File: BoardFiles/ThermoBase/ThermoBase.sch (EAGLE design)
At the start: 31 parts, among them CON1 BARREL_JACK_3PIN, U1 MOSFET_N, U2 MOSFET_N, U3 MOSFET_N, U4 LM317

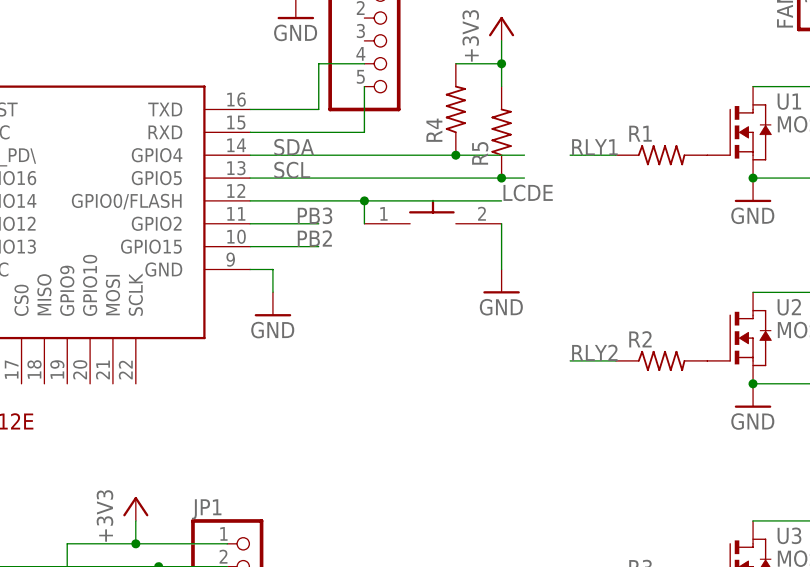
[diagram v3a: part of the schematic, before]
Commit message: Found some board errors and got an AC demo ready
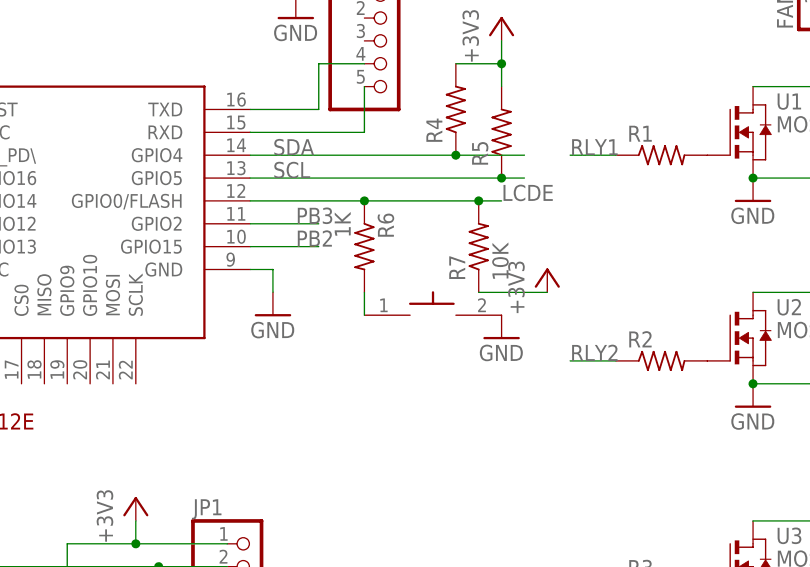
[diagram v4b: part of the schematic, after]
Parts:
- added R6: 1K, DR:R-US_R0805
- added R7: 10K, DR:R-US_R0805
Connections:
- new net N$16: BTN1.P$1, R6.2
- net +3V3: now also R7.1
- net LCDE: now also R6.1, R7.2; no longer BTN1.P$1
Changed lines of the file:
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@@
 <part name="+3V6" library="supply1" library_urn="urn:adsk.eagle:library:371" deviceset="+3V3" device=""/>
 <part name="GND12" library="supply1" library_urn="urn:adsk.eagle:library:371" deviceset="GND" device=""/>
+<part name="R6" library="DR" deviceset="R-US_" device="R0805" value="1K"/>
+<part name="R7" library="DR" deviceset="R-US_" device="R0805" value="10K"/>
+<part name="+3V7" library="supply1" library_urn="urn:adsk.eagle:library:371" deviceset="+3V3" device=""/>
 </parts>
 <sheets>
@@
 <attribute name="VALUE" x="91.44" y="60.96" size="1.778" layer="96"/>
 </instance>
-<instance part="BTN1" gate="G$1" x="109.22" y="40.64" smashed="yes"/>
-<instance part="GND2" gate="1" x="116.84" y="33.02" smashed="yes">
-<attribute name="VALUE" x="114.3" y="30.48" size="1.778" layer="96"/>
+<instance part="BTN1" gate="G$1" x="109.22" y="30.48" smashed="yes"/>
+<instance part="GND2" gate="1" x="116.84" y="27.94" smashed="yes">
+<attribute name="VALUE" x="114.3" y="25.4" size="1.778" layer="96"/>
 </instance>
 <instance part="+3V1" gate="G$1" x="45.72" y="58.42" smashed="yes">
@@
 <instance part="GND12" gate="1" x="60.96" y="0" smashed="yes">
 <attribute name="VALUE" x="58.42" y="-2.54" size="1.778" layer="96"/>
+</instance>
+<instance part="R6" gate="G$1" x="101.6" y="38.1" smashed="yes" rot="R270">
+<attribute name="NAME" x="103.0986" y="41.91" size="1.778" layer="95" rot="R270"/>
+<attribute name="VALUE" x="98.298" y="41.91" size="1.778" layer="96" rot="R270"/>
+</instance>
+<instance part="R7" gate="G$1" x="114.3" y="38.1" smashed="yes" rot="R90">
+<attribute name="NAME" x="112.8014" y="34.29" size="1.778" layer="95" rot="R90"/>
+<attribute name="VALUE" x="117.602" y="34.29" size="1.778" layer="96" rot="R90"/>
+</instance>
+<instance part="+3V7" gate="G$1" x="121.92" y="35.56" smashed="yes">
+<attribute name="VALUE" x="119.38" y="30.48" size="1.778" layer="96" rot="R90"/>
 </instance>
 </instances>
@@
 <pinref part="BTN1" gate="G$1" pin="P$2"/>
 <pinref part="GND2" gate="1" pin="GND"/>
-<wire x1="116.84" y1="35.56" x2="116.84" y2="40.64" width="0.1524" layer="91"/>
 </segment>
 <segment>
@@
 <wire x1="68.58" y1="-12.7" x2="86.36" y2="-12.7" width="0.1524" layer="91"/>
 </segment>
+<segment>
+<pinref part="+3V7" gate="G$1" pin="+3V3"/>
+<pinref part="R7" gate="G$1" pin="1"/>
+<wire x1="121.92" y1="33.02" x2="114.3" y2="33.02" width="0.1524" layer="91"/>
+</segment>
 </net>
 <net name="SDA" class="0">
@@
 </segment>
 <segment>
-<pinref part="BTN1" gate="G$1" pin="P$1"/>
 <pinref part="U$1" gate="G$1" pin="GPIO0/FLASH"/>
-<wire x1="101.6" y1="40.64" x2="101.6" y2="43.18" width="0.1524" layer="91"/>
-<wire x1="101.6" y1="43.18" x2="88.9" y2="43.18" width="0.1524" layer="91"/>
-<wire x1="101.6" y1="43.18" x2="116.84" y2="43.18" width="0.1524" layer="91"/>
+<wire x1="88.9" y1="43.18" x2="101.6" y2="43.18" width="0.1524" layer="91"/>
+<label x="116.84" y="43.18" size="1.778" layer="95"/>
+<pinref part="R6" gate="G$1" pin="1"/>
+<wire x1="101.6" y1="43.18" x2="114.3" y2="43.18" width="0.1524" layer="91"/>
 <junction x="101.6" y="43.18"/>
-<label x="116.84" y="43.18" size="1.778" layer="95"/>
+<pinref part="R7" gate="G$1" pin="2"/>
+<wire x1="114.3" y1="43.18" x2="116.84" y2="43.18" width="0.1524" layer="91"/>
+<junction x="114.3" y="43.18"/>
 </segment>
 </net>
@@
 </segment>
 </net>
+<net name="N$16" class="0">
+<segment>
+<pinref part="BTN1" gate="G$1" pin="P$1"/>
+<pinref part="R6" gate="G$1" pin="2"/>
+<wire x1="101.6" y1="30.48" x2="101.6" y2="33.02" width="0.1524" layer="91"/>
+</segment>
+</net>

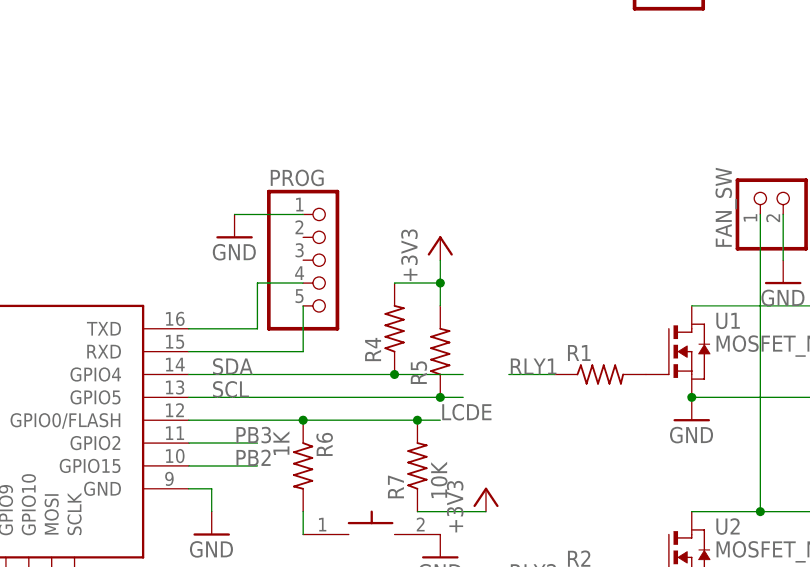
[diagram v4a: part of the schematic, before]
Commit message: Ordered boards V1.0
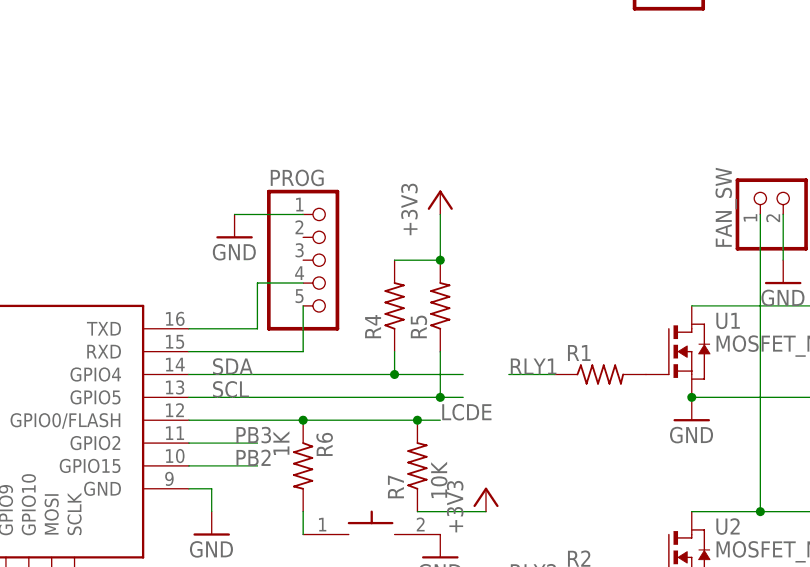
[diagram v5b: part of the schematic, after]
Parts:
- CON1: value BARREL_JACK_3PIN -> BARREL_JACK_3PINPJ-102A_2MM_HOLES; device DR:BARREL_JACK_3PIN -> DR:BARREL_JACK_3PINPJ-102A_2MM_HOLES
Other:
- moved on the sheet: R4, R5
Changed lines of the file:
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@@
 <layer number="56" name="wert" color="7" fill="1" visible="no" active="no"/>
 <layer number="57" name="tCAD" color="7" fill="1" visible="no" active="no"/>
+<layer number="88" name="SimResults" color="9" fill="1" visible="no" active="no"/>
+<layer number="89" name="SimProbes" color="9" fill="1" visible="no" active="no"/>
 <layer number="90" name="Modules" color="5" fill="1" visible="no" active="no"/>
 <layer number="91" name="Nets" color="2" fill="1" visible="yes" active="yes"/>
@@
 <part name="+3V3" library="supply1" library_urn="urn:adsk.eagle:library:371" deviceset="+3V3" device=""/>
 <part name="GND3" library="supply1" library_urn="urn:adsk.eagle:library:371" deviceset="GND" device=""/>
-<part name="CON1" library="DR" deviceset="BARREL_JACK_3PIN" device=""/>
+<part name="CON1" library="DR" deviceset="BARREL_JACK_3PIN" device="PJ-102A_2MM_HOLES" value="BARREL_JACK_3PINPJ-102A_2MM_HOLES"/>
 <part name="C1" library="DR" deviceset="C-US" device="C0805"/>
 <part name="C2" library="DR" deviceset="C-US" device="C0805"/>
@@
 <attribute name="VALUE" x="20.32" y="60.96" size="1.778" layer="96"/>
 </instance>
-<instance part="R4" gate="G$1" x="111.76" y="53.34" smashed="yes" rot="R90">
-<attribute name="NAME" x="110.2614" y="49.53" size="1.778" layer="95" rot="R90"/>
-<attribute name="VALUE" x="115.062" y="49.53" size="1.778" layer="96" rot="R90"/>
-</instance>
-<instance part="R5" gate="G$1" x="116.84" y="50.8" smashed="yes" rot="R90">
-<attribute name="NAME" x="115.3414" y="46.99" size="1.778" layer="95" rot="R90"/>
-<attribute name="VALUE" x="120.142" y="46.99" size="1.778" layer="96" rot="R90"/>
+<instance part="R4" gate="G$1" x="111.76" y="55.88" smashed="yes" rot="R90">
+<attribute name="NAME" x="110.2614" y="52.07" size="1.778" layer="95" rot="R90"/>
+<attribute name="VALUE" x="115.062" y="52.07" size="1.778" layer="96" rot="R90"/>
+</instance>
+<instance part="R5" gate="G$1" x="116.84" y="55.88" smashed="yes" rot="R90">
+<attribute name="NAME" x="115.3414" y="52.07" size="1.778" layer="95" rot="R90"/>
+<attribute name="VALUE" x="120.142" y="52.07" size="1.778" layer="96" rot="R90"/>
 </instance>
 <instance part="JP3" gate="A" x="20.32" y="10.16" smashed="yes">
@@
 <attribute name="VALUE" x="27.94" y="-5.08" size="1.778" layer="96"/>
 </instance>
-<instance part="+3V5" gate="G$1" x="116.84" y="63.5" smashed="yes">
-<attribute name="VALUE" x="114.3" y="58.42" size="1.778" layer="96" rot="R90"/>
+<instance part="+3V5" gate="G$1" x="116.84" y="68.58" smashed="yes">
+<attribute name="VALUE" x="114.3" y="63.5" size="1.778" layer="96" rot="R90"/>
 </instance>
 <instance part="RLY1" gate="G$1" x="190.5" y="58.42" smashed="yes">
@@
 <pinref part="R5" gate="G$1" pin="2"/>
 <pinref part="+3V5" gate="G$1" pin="+3V3"/>
-<wire x1="116.84" y1="55.88" x2="116.84" y2="58.42" width="0.1524" layer="91"/>
 <pinref part="R4" gate="G$1" pin="2"/>
-<wire x1="116.84" y1="58.42" x2="116.84" y2="60.96" width="0.1524" layer="91"/>
-<wire x1="116.84" y1="58.42" x2="111.76" y2="58.42" width="0.1524" layer="91"/>
-<junction x="116.84" y="58.42"/>
+<wire x1="116.84" y1="60.96" x2="116.84" y2="66.04" width="0.1524" layer="91"/>
+<wire x1="116.84" y1="60.96" x2="111.76" y2="60.96" width="0.1524" layer="91"/>
+<junction x="116.84" y="60.96"/>
 </segment>
 <segment>
@@
 <pinref part="R4" gate="G$1" pin="1"/>
 <wire x1="88.9" y1="48.26" x2="111.76" y2="48.26" width="0.1524" layer="91"/>
+<wire x1="111.76" y1="50.8" x2="111.76" y2="48.26" width="0.1524" layer="91"/>
 <wire x1="111.76" y1="48.26" x2="119.38" y2="48.26" width="0.1524" layer="91"/>
 <junction x="111.76" y="48.26"/>
@@
 <pinref part="R5" gate="G$1" pin="1"/>
 <wire x1="88.9" y1="45.72" x2="116.84" y2="45.72" width="0.1524" layer="91"/>
+<wire x1="116.84" y1="45.72" x2="116.84" y2="50.8" width="0.1524" layer="91"/>
+<junction x="116.84" y="45.72"/>
 <wire x1="116.84" y1="45.72" x2="119.38" y2="45.72" width="0.1524" layer="91"/>
-<junction x="116.84" y="45.72"/>
-</segment>
-<segment>
+</segment>
+<segment>
